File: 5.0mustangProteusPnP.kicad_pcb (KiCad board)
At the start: 2 copper layers, 139.7 x 111.1 mm, 7 parts, among them J1 5-146280-3, J2 5103308-3, J3 776228-1, J4 5103308-3, J5 776231-2, J6 776231-1, U1 FORD60PIN

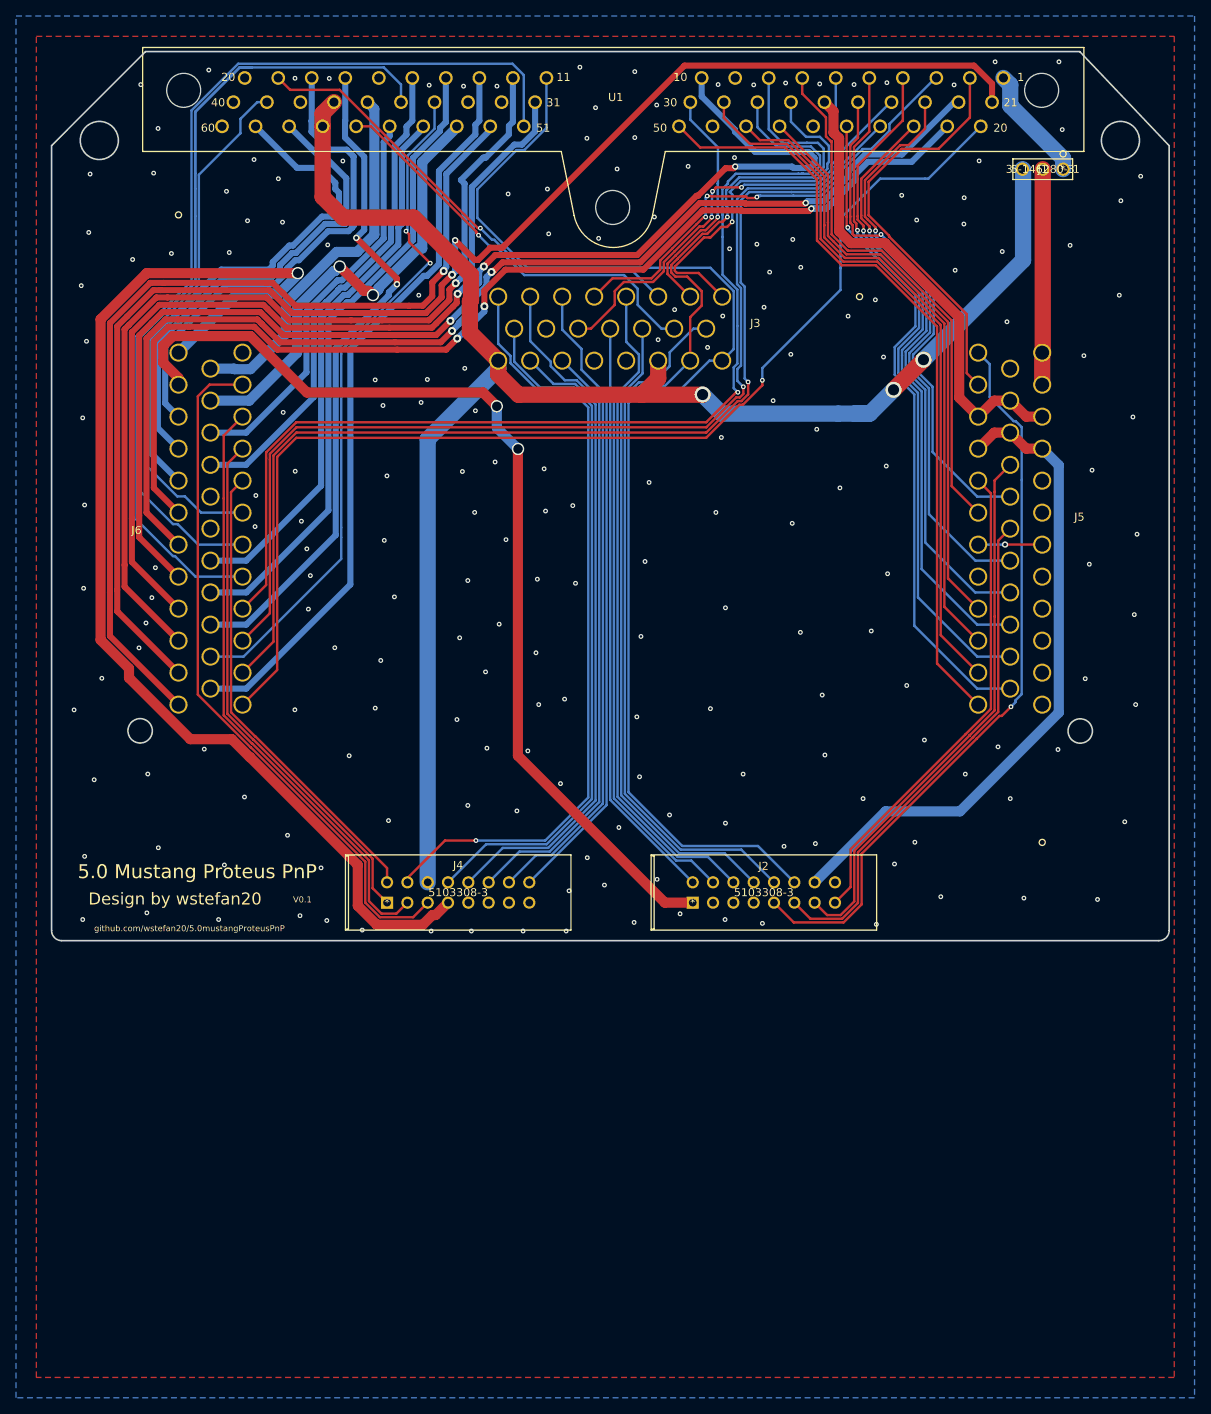
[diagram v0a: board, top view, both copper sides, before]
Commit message: update
обновила до 6.0, поставила современный футпринт
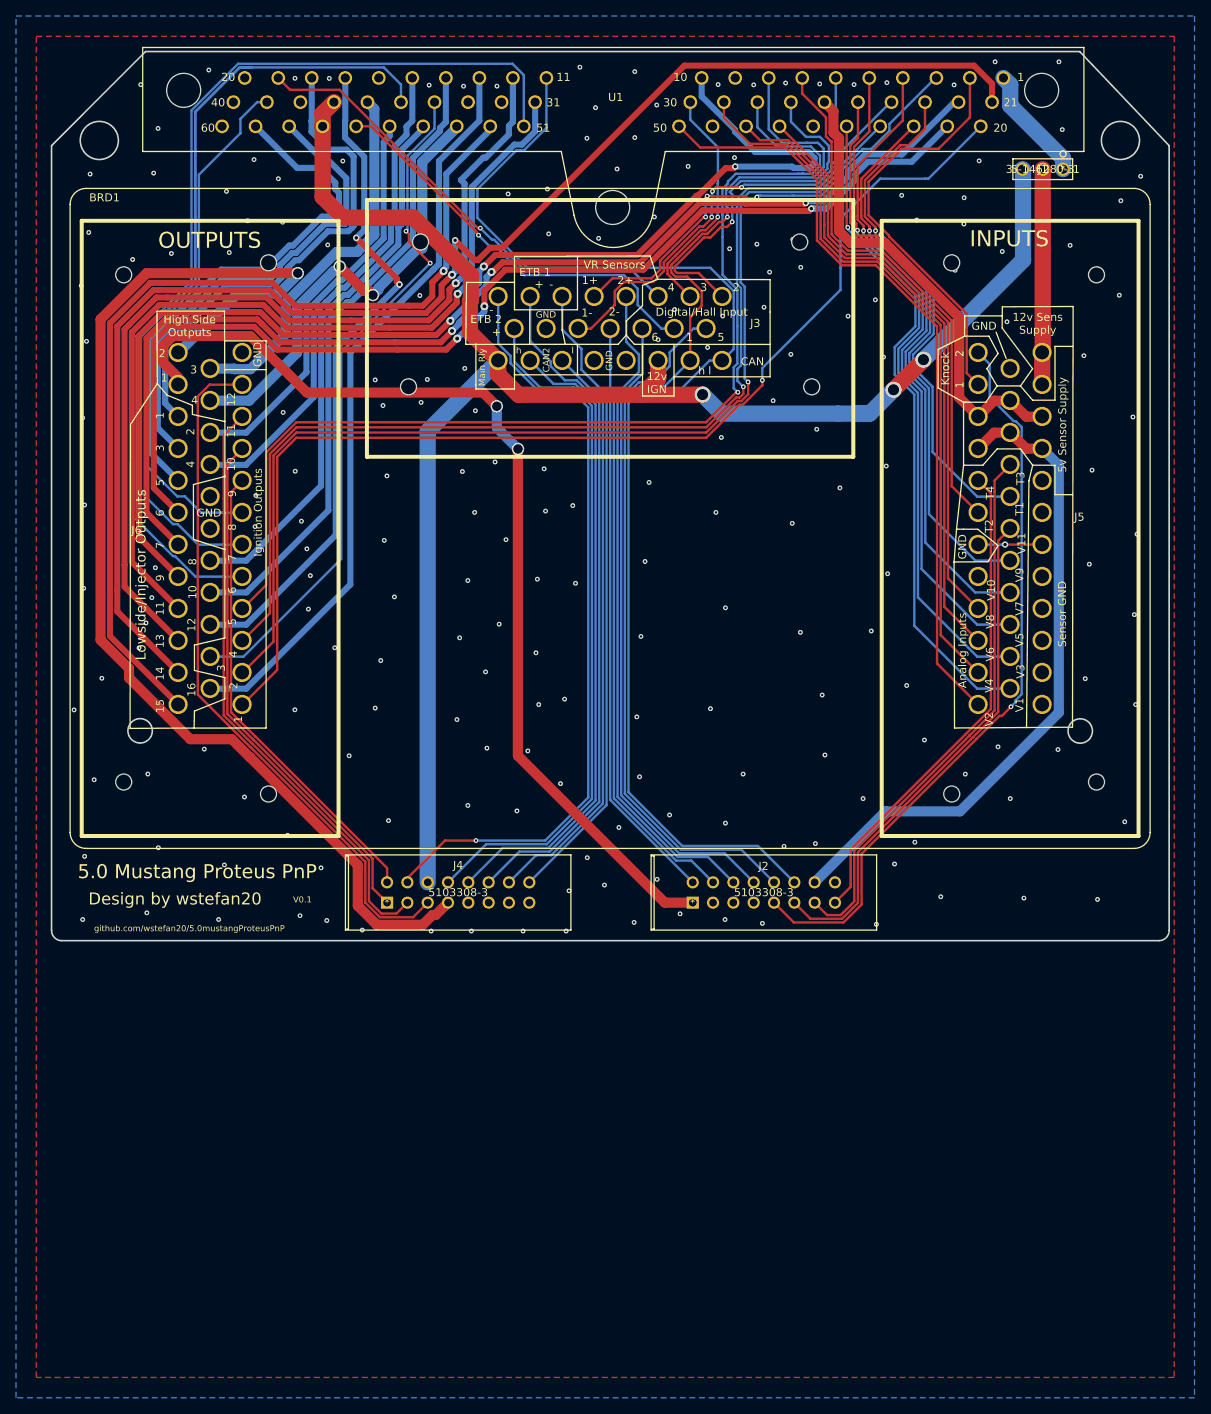
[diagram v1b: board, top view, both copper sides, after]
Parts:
- removed J3: 776228-1, 776228-1:776228-1
- removed J5: 776231-2, 776231-2:776231-2
- removed J6: 776231-1, 776231-1:776231-1
- added BRD1: proteus, Connector_Molex:proteus, F.Cu at (98.2, 162.4)
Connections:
- J2 pad 3: (no net) -> unconnected-(J2-Pad3)
- J2 pad 5: (no net) -> unconnected-(J2-Pad5)
- J2 pad 7: (no net) -> unconnected-(J2-Pad7)
- J4 pad 11: (no net) -> unconnected-(J4-Pad11)
- J4 pad 13: (no net) -> unconnected-(J4-Pad13)
- J4 pad 15: (no net) -> unconnected-(J4-Pad15)
- J4 pad 9: (no net) -> unconnected-(J4-Pad9)
- U1 pad 32: (no net) -> unconnected-(U1-Pad32)
- U1 pad 33: (no net) -> unconnected-(U1-Pad33)
- U1 pad 38: (no net) -> unconnected-(U1-Pad38)
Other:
- net class Default removed
- net class traces_50_mils removed

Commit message: add WBO module in sch
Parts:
- added J10: XH-10AW, Connector_JST:JST_XH_S10B-XH-A_1x10_P2.50mm_Horizontal, F.Cu at (226.2, 194.8)
- added J13: Conn_01x06, Connector_PinHeader_2.54mm:PinHeader_1x06_P2.54mm_Vertical, F.Cu at (186.4, 219.1)
- added J3: Conn_01x06, Connector_PinHeader_2.54mm:PinHeader_1x06_P2.54mm_Vertical, F.Cu at (186.4, 195.0)
- added J7: XH-10AW, Connector_JST:JST_XH_S10B-XH-A_1x10_P2.50mm_Horizontal, F.Cu at (226.2, 223.3)
- added M1: Module-wbo-0.3, hellen-one-wbo-0.3:wbo, F.Cu at (176.6, 216.6)
- added M2: Module-can-0.1, hellen-one-can-0.1:can, F.Cu at (167.8, 177.6)
- added M3: Module-wbo-0.3, hellen-one-wbo-0.3:wbo, F.Cu at (176.7, 192.5)
- added M4: Module-can-0.1, hellen-one-can-0.1:can, F.Cu at (167.8, 201.6)
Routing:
- net /12V_MR: track 211.8 -> 297.6 mm, vias 3 -> 5
- net /IGN3: track 85.8 -> 0.00 mm, vias 2 -> 0

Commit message: трассировка
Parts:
- moved J7 126.9 mm to (107.4, 178.6), turned to -90 degrees
- moved J13 60.0 mm to (141.5, 179.3), turned to 90 degrees
- moved M1 39.6 mm to (155.9, 182.8), turned to 180 degrees
- moved J3 7.60 mm to (191.4, 200.8)
- moved M2 6.99 mm to (167.1, 184.6)
- moved J10 6.71 mm to (224.0, 201.1)
- moved M4 6.36 mm to (164.8, 195.9), turned to 90 degrees
- moved M3 5.18 mm to (176.5, 197.6)
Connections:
- BRD1 pad B18(21): unconnected-(BRD1-PadB18(21)) -> /12V_MR
- M2 pad S1: /CAN_L -> /CAN-
- M2 pad S2: /CAN_H -> /CAN+
- M4 pad S1: /CAN_L -> /CAN-
- M4 pad S2: /CAN_H -> /CAN+
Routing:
- net /12V_MR: track 297.6 -> 401.4 mm, vias 5 -> 3
- net /IGN3: track 0.00 -> 88.4 mm, vias 0 -> 2
- net /CAN-: track 154.7 -> 202.0 mm, vias 0 -> 1
- net /IGN7: track 132.9 -> 99.4 mm
- net +5VA: track 0.00 -> 29.9 mm
- net /CAN+: track 140.5 -> 169.6 mm, vias 1 -> 3
- net Net-(J3-Pad2): track 0.00 -> 20.1 mm
- net Net-(J3-Pad1): track 0.00 -> 19.5 mm
- net Net-(J13-Pad2): track 0.00 -> 19.0 mm
- net Net-(J13-Pad1): track 0.00 -> 18.9 mm
- net /DIGITAL_2: track 45.9 -> 28.5 mm
- net Net-(J3-Pad4): track 0.00 -> 16.5 mm
- net Net-(J13-Pad4): track 0.00 -> 15.3 mm
- net Net-(J3-Pad5): track 0.00 -> 15.2 mm
- net Net-(J7-Pad7): track 0.00 -> 15.1 mm
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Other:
- board size 139.7 x 111.1 mm -> 139.7 x 149.6 mm

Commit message: add export files
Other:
- board text added: "V0.2re"
- board text added: "github.com/rusefi/proteus-mustang5.0-60-pin"
- board text removed: "V0.1"
- board text removed: "github.com/wstefan20/5.0mustangProteusPnP"
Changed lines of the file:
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@@
     )
     (pad_to_mask_clearance 0.000076)
-    (grid_origin 107.6381 62.865)
+    (grid_origin 95.885 212.471)
     (pcbplotparams
-      (layerselection 0x00010f0_ffffffff)
-      (disableapertmacros false)
+      (layerselection 0x00010f8_ffffffff)
+      (disableapertmacros true)
       (usegerberextensions true)
       (usegerberattributes false)
-      (usegerberadvancedattributes false)
-      (creategerberjobfile true)
+      (usegerberadvancedattributes true)
+      (creategerberjobfile false)
       (svguseinch false)
       (svgprecision 6)
-      (excludeedgelayer true)
+      (excludeedgelayer false)
       (plotframeref false)
       (viasonmask false)
       (mode 1)
-      (useauxorigin false)
+      (useauxorigin true)
       (hpglpennumber 1)
       (hpglpenspeed 20)
@@
       (psnegative false)
       (psa4output false)
-      (plotreference false)
+      (plotreference true)
       (plotvalue false)
       (plotinvisibletext false)
@@
       (drillshape 0)
       (scaleselection 1)
-      (outputdirectory "export/")
+      (outputdirectory "export_19_05_2022/")
     )
   )
@@
     (effects (font (size 1.016 1.016) (thickness 0.13)))
   )
-  (gr_text "V0.1" (at 127.23876 168.8719) (layer "F.SilkS")
+  (gr_text "V0.2re" (at 127.23876 168.8719) (layer "F.SilkS")
     (effects (font (size 0.75 0.75) (thickness 0.13)))
   )
@@
     (effects (font (size 1.016 1.016) (thickness 0.13)))
   )
-  (gr_text "github.com/wstefan20/5.0mustangProteusPnP" (at 113.11636 172.47362) (layer "F.SilkS")
+  (gr_text "github.com/rusefi/proteus-mustang5.0-60-pin" (at 113.11636 172.47362) (layer "F.SilkS")
     (effects (font (size 0.75 0.75) (thickness 0.13)))
   )
@@
   (via (at 115.53952 65.17386) (size 0.6) (drill 0.3) (layers "F.Cu" "B.Cu") (net 1))
   (via (at 173.13402 158.2928) (size 0.6) (drill 0.3) (layers "F.Cu" "B.Cu") (net 1))
-  (via (at 130.29184 171.48302) (size 0.6) (drill 0.3) (layers "F.Cu" "B.Cu") (net 1))
+  (via (at 129.7361 172.339) (size 0.6) (drill 0.3) (layers "F.Cu" "B.Cu") (net 1))
   (via (at 217.195619 124.000104) (size 0.78994) (drill 0.43434) (layers "F.Cu" "B.Cu") (net 1))
   (via (at 189.5348 89.83726) (size 0.6) (drill 0.3) (layers "F.Cu" "B.Cu") (net 1))
@@
   (segment (start 151.54148 109.88548) (end 154.19324 112.53724) (width 1.27) (layer "B.Cu") (net 69))
   (segment (start 151.54148 107.20324) (end 151.54148 109.88548) (width 1.27) (layer "B.Cu") (net 69))
-  (segment (start 99.822 139.446) (end 130.619709 170.243709) (width 1.27) (layer "F.Cu") (net 70))
+  (segment (start 132.39244 172.01644) (end 142.67733 172.01644) (width 1.27) (layer "F.Cu") (net 70))
+  (segment (start 142.67733 172.01644) (end 145.44341 169.25036) (width 1.27) (layer "F.Cu") (net 70))
+  (segment (start 99.822 139.446) (end 132.39244 172.01644) (width 1.27) (layer "F.Cu") (net 70))
+  (segment (start 104.267 86.106) (end 99.822 90.551) (width 1.27) (layer "F.Cu") (net 70))
   (segment (start 99.822 90.551) (end 99.822 139.446) (width 1.27) (layer "F.Cu") (net 70))
+  (segment (start 126.662026 90.566086) (end 126.662026 88.181026) (width 1.27) (layer "F.Cu") (net 70))
   (segment (start 124.587 86.106) (end 104.267 86.106) (width 1.27) (layer "F.Cu") (net 70))
   (segment (start 126.662026 88.181026) (end 124.587 86.106) (width 1.27) (layer "F.Cu") (net 70))
-  (segment (start 142.67733 172.01644) (end 145.44341 169.25036) (width 1.27) (layer "F.Cu") (net 70))
-  (segment (start 131.531151 171.155151) (end 132.39244 172.01644) (width 1.27) (layer "F.Cu") (net 70))
-  (segment (start 126.662026 90.566086) (end 126.662026 88.181026) (width 1.27) (layer "F.Cu") (net 70))
-  (segment (start 131.531151 170.969679) (end 131.531151 171.155151) (width 1.27) (layer "F.Cu") (net 70))
-  (segment (start 130.805181 170.243709) (end 131.531151 170.969679) (width 1.27) (layer "F.Cu") (net 70))
-  (segment (start 104.267 86.106) (end 99.822 90.551) (width 1.27) (layer "F.Cu") (net 70))
-  (segment (start 130.619709 170.243709) (end 130.805181 170.243709) (width 1.27) (layer "F.Cu") (net 70))
-  (segment (start 132.39244 172.01644) (end 142.67733 172.01644) (width 1.27) (layer "F.Cu") (net 70))
   (via (at 126.662026 90.566086) (size 1.54178) (drill 1.18618) (layers "F.Cu" "B.Cu") (net 70))
   (segment (start 126.662026 90.758252) (end 126.662026 90.566086) (width 1.27) (layer "B.Cu") (net 70))
